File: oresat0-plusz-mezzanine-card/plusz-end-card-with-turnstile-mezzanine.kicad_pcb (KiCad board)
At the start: 8 copper layers, 83 x 84.4 mm, 37 parts, among them J1 R107064070, J10 R107064070, J2 R107064070, J3 R107064070, J4 R107064070, J5 R107064070, J6 R107064070, J7 R107064070, J8 R107064070, J9 R107064070, U1 QBA-07+, U2 QBA-07+, U3 QBA-07+, U7 QCN-19+, U8 QCN-19+, U9 QCN-19+

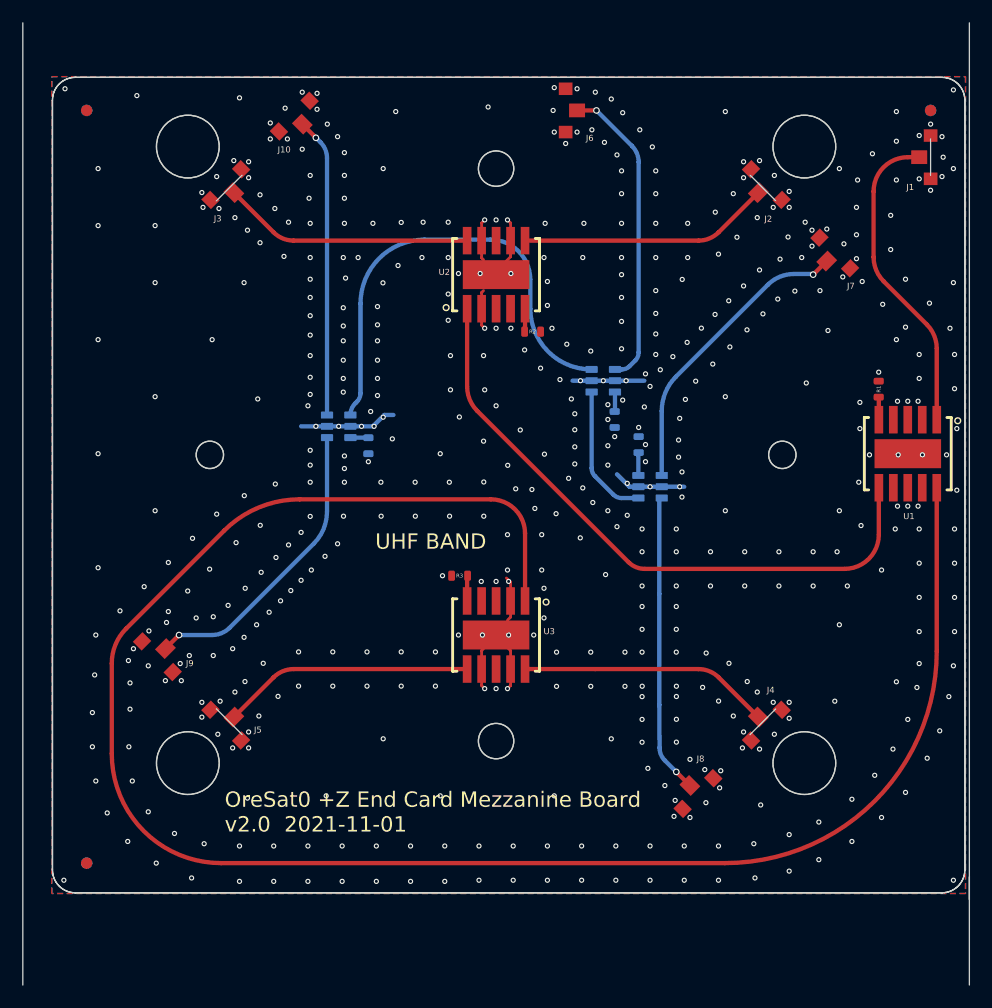
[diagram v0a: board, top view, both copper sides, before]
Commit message: Fixed Board Outline
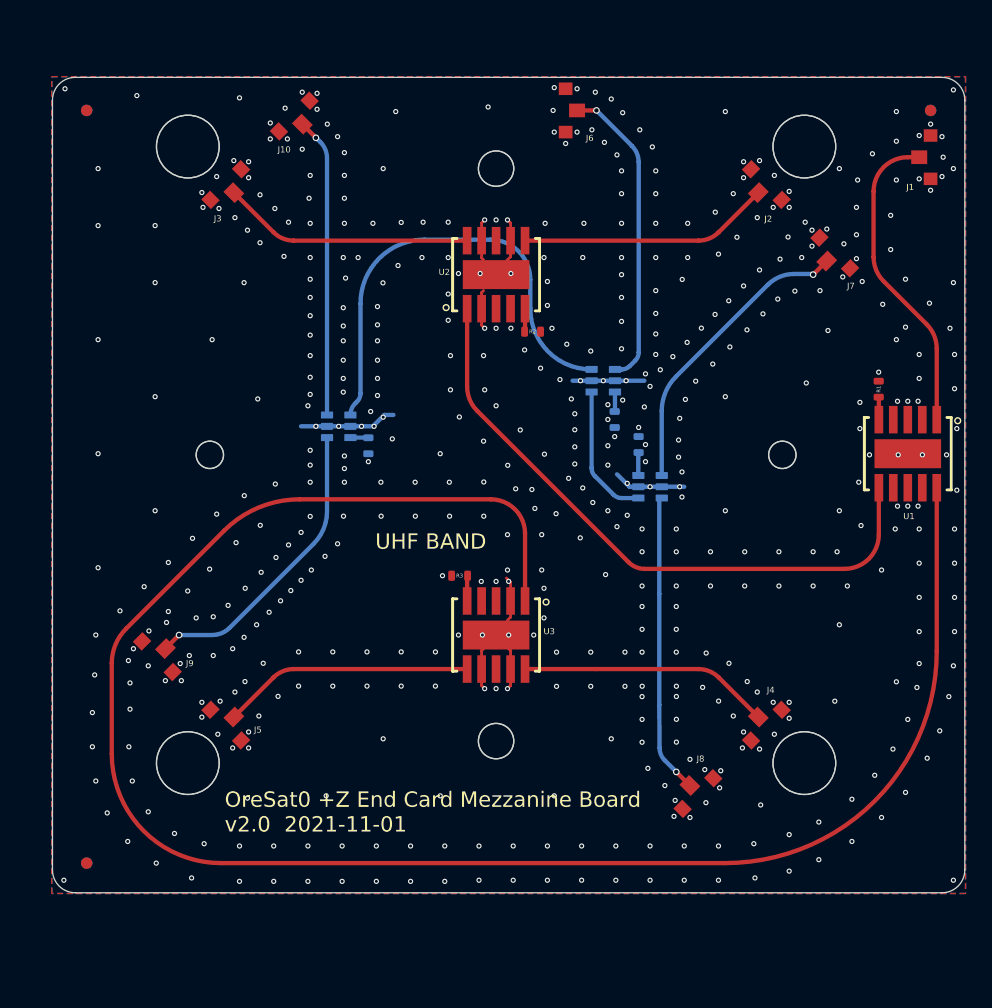
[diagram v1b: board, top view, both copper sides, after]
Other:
- board size 83 x 84.4 mm -> 80 x 71.5 mm
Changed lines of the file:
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@@
 		(descr "0603 (metric 1608) tight 'IPC-C' without silkscreen\nIn house package for minimum spacing based on IPC-7351B. This package is identical to 0603-C, but has its tPlace silkscreen layer removed.")
 		(property "Reference" "R5"
-			(at 0 0 -90)
+			(at 0 0 270)
 			(unlocked yes)
 			(layer "B.SilkS")
@@
 		)
 		(property "Value" "50"
-			(at -1.5 -1.8 -90)
+			(at -1.5 -1.8 270)
 			(unlocked yes)
 			(layer "B.Fab")
@@
 		)
 		(property "Datasheet" ""
-			(at 0 0 -90)
+			(at 0 0 270)
 			(layer "B.Fab")
 			(hide yes)
@@
 		)
 		(property "Description" ""
-			(at 0 0 -90)
+			(at 0 0 270)
 			(layer "B.Fab")
 			(hide yes)
@@
 		(at 134.7011 98.198579 -90)
 		(property "Reference" "U9"
-			(at -0.5 2.6 -0)
+			(at -0.5 2.6 0)
 			(unlocked yes)
 			(layer "B.SilkS")
@@
 		)
 		(property "Value" "QCN-19+"
-			(at 3.3 -1.4 -0)
+			(at 3.3 -1.4 0)
 			(unlocked yes)
 			(layer "B.Fab")
@@
 		(descr "0603 (metric 1608) tight 'IPC-C' without silkscreen\nIn house package for minimum spacing based on IPC-7351B. This package is identical to 0603-C, but has its tPlace silkscreen layer removed.")
 		(property "Reference" "R4"
-			(at 0 0 -90)
+			(at 0 0 270)
 			(unlocked yes)
 			(layer "B.SilkS")
@@
 		)
 		(property "Value" "50"
-			(at -1.5 -1.8 -90)
+			(at -1.5 -1.8 270)
 			(unlocked yes)
 			(layer "B.Fab")
@@
 		)
 		(property "Datasheet" ""
-			(at 0 0 -90)
+			(at 0 0 270)
 			(layer "B.Fab")
 			(hide yes)
@@
 		)
 		(property "Description" ""
-			(at 0 0 -90)
+			(at 0 0 270)
 			(layer "B.Fab")
 			(hide yes)
@@
 		)
 		(fp_text user "${REFERENCE}"
-			(at 0 0 -90)
+			(at 0 0 270)
 			(unlocked yes)
 			(layer "B.Mask")
@@
 		(at 157.9011 94.198579 -90)
 		(property "Reference" "U7"
-			(at -0.7 2.7 -0)
+			(at -0.7 2.7 0)
 			(unlocked yes)
 			(layer "B.SilkS")
@@
 		)
 		(property "Value" "QCN-19+"
-			(at 3.3 -1.4 -0)
+			(at 3.3 -1.4 0)
 			(unlocked yes)
 			(layer "B.Fab")
@@
 		(descr "0603 (metric 1608) tight 'IPC-C' without silkscreen\nIn house package for minimum spacing based on IPC-7351B. This package is identical to 0603-C, but has its tPlace silkscreen layer removed.")
 		(property "Reference" "R6"
-			(at 0 0 -90)
+			(at 0 0 270)
 			(unlocked yes)
 			(layer "B.SilkS")
@@
 		)
 		(property "Value" "50"
-			(at -1.5 -1.8 -90)
+			(at -1.5 -1.8 270)
 			(unlocked yes)
 			(layer "B.Fab")
@@
 		)
 		(property "Datasheet" ""
-			(at 0 0 -90)
+			(at 0 0 270)
 			(layer "B.Fab")
 			(hide yes)
@@
 		)
 		(property "Description" ""
-			(at 0 0 -90)
+			(at 0 0 270)
 			(layer "B.Fab")
 			(hide yes)
@@
 		)
 		(fp_text user "${REFERENCE}"
-			(at 0 0 -90)
+			(at 0 0 270)
 			(unlocked yes)
 			(layer "B.Mask")
@@
 		(end 176.1011 100.698579)
 		(stroke
-			(width 0)
+			(width 0.1)
 			(type solid)
 		)
@@
 		(end 151.5011 125.798579)
 		(stroke
-			(width 0)
+			(width 0.1)
 			(type solid)
 		)
@@
 		(end 158.1011 70.498579)
 		(stroke
-			(width 0)
+			(width 0.1)
 			(type solid)
 		)
@@
 		(end 165.1011 128.498579)
 		(stroke
-			(width 0)
+			(width 0.1)
 			(type solid)
 		)
@@
 		(end 177.1011 84.898579)
 		(stroke
-			(width 0)
+			(width 0.1)
 			(type solid)
 		)
@@
 		(end 125.9011 100.698579)
 		(stroke
-			(width 0)
+			(width 0.1)
 			(type solid)
 		)
@@
 		(end 121.5011 116.498579)
 		(stroke
-			(width 0)
+			(width 0.1)
 			(type solid)
 		)
@@
 		(end 151.5011 75.598579)
 		(stroke
-			(width 0)
+			(width 0.1)
 			(type solid)
 		)
@@
 		(end 133.5011 72.898579)
 		(stroke
-			(width 0)
+			(width 0.1)
 			(type solid)
 		)
@@
 		(end 126.4011 100.698579)
 		(stroke
-			(width 0)
+			(width 0.1)
 			(type solid)
 		)
@@
 		(end 151.5011 75.598579)
 		(stroke
-			(width 0)
+			(width 0.1)
 			(type solid)
 		)
@@
 		(end 151.5011 125.798579)
 		(stroke
-			(width 0)
+			(width 0.1)
 			(type solid)
 		)
@@
 		(end 176.6011 100.698579)
 		(stroke
-			(width 0)
+			(width 0.1)
 			(type solid)
 		)
@@
 		(layer "B.Mask")
 	)
-	(gr_line
-		(start 109.6011 137.098579)
-		(end 109.6011 69.598579)
-		(stroke
-			(width 0.001)
-			(type solid)
-		)
-		(layer "Edge.Cuts")
-	)
 	(gr_circle
 		(center 123.40109 100.698589)
@@
 	)
 	(gr_line
-		(start 186.60109 72.998589)
-		(end 186.60109 76.198589)
-		(stroke
-			(width 0.001)
-			(type solid)
-		)
-		(layer "Edge.Cuts")
-	)
-	(gr_line
-		(start 173.032459 78.429961)
-		(end 170.769718 76.16722)
-		(stroke
-			(width 0.001)
-			(type solid)
-		)
-		(layer "Edge.Cuts")
-	)
-	(gr_line
-		(start 170.769718 125.229939)
-		(end 173.032459 122.967198)
-		(stroke
-			(width 0.001)
-			(type solid)
-		)
-		(layer "Edge.Cuts")
-	)
-	(gr_arc
-		(start 189.6011 137.098579)
-		(mid 189.015314 138.512793)
-		(end 187.6011 139.098579)
-		(stroke
-			(width 0.001)
-			(type solid)
-		)
-		(layer "Edge.Cuts")
-	)
-	(gr_arc
-		(start 187.6011 67.598579)
-		(mid 189.015314 68.184365)
-		(end 189.6011 69.598579)
-		(stroke
-			(width 0.001)
-			(type solid)
-		)
-		(layer "Edge.Cuts")
-	)
-	(gr_line
-		(start 189.6011 137.098579)
-		(end 189.6011 69.598579)
-		(stroke
-			(width 0.001)
-			(type solid)
-		)
-		(layer "Edge.Cuts")
-	)
-	(gr_line
-		(start 107.0011 62.815761)
-		(end 107.0011 147.191439)
-		(stroke
-			(width 0.001)
-			(type solid)
-		)
-		(layer "Edge.Cuts")
-	)
-	(gr_arc
-		(start 109.6011 69.598579)
-		(mid 110.186886 68.184365)
-		(end 111.6011 67.598579)
-		(stroke
-			(width 0.001)
-			(type solid)
-		)
-		(layer "Edge.Cuts")
-	)
-	(gr_line
-		(start 187.6011 139.098579)
-		(end 111.6011 139.098579)
-		(stroke
-			(width 0.001)
-			(type solid)
-		)
-		(layer "Edge.Cuts")
-	)
-	(gr_line
 		(start 189.6011 69.598579)
 		(end 189.6011 137.098579)
@@
 		(layer "Edge.Cuts")
 	)
-	(gr_line
-		(start 190.0011 137.698579)
-		(end 190.0011 139.698579)
-		(stroke
-			(width 0.001)
-			(type solid)
-		)
-		(layer "Edge.Cuts")
-	)
-	(gr_line
-		(start 123.96974 122.967198)
-		(end 126.232481 125.229939)
-		(stroke
-			(width 0.001)
-			(type solid)
-		)
-		(layer "Edge.Cuts")
-	)
 	(gr_arc
 		(start 187.6011 67.598579)
@@
 		(layer "Edge.Cuts")
 	)
-	(gr_line
-		(start 187.6011 67.598579)
-		(end 111.6011 67.598579)
-		(stroke
-			(width 0.001)
-			(type solid)
-		)
-		(layer "Edge.Cuts")
-	)
 	(gr_arc
 		(start 109.6011 69.598579)
@@
 		(layer "Edge.Cuts")
 	)
-	(gr_line
-		(start 190.0011 62.815761)
-		(end 190.0011 147.191439)
-		(stroke
-			(width 0.001)
-			(type solid)
-		)
-		(layer "Edge.Cuts")
-	)
 	(gr_circle
 		(center 175.5311 73.668579)
@@
 		(layer "Edge.Cuts")
 	)
-	(gr_line
-		(start 126.232481 76.16722)
-		(end 123.96974 78.429961)
-		(stroke
-			(width 0.001)
-			(type solid)
-		)
-		(layer "Edge.Cuts")
-	)
 	(gr_arc
 		(start 111.6011 139.098579)
@@
 		(layer "Edge.Cuts")
 	)
-	(gr_arc
-		(start 111.6011 139.098579)
-		(mid 110.186886 138.512793)
-		(end 109.6011 137.098579)
-		(stroke
-			(width 0.001)
-			(type solid)
-		)
-		(layer "Edge.Cuts")
-	)
 	(gr_circle
 		(center 148.5011 91.398579)
@@
 				(xy 124.173642 103.07622) (xy 124.465548 102.960647) (xy 124.740667 102.809399) (xy 124.99466 102.624862)
 				(xy 125.223522 102.409947) (xy 125.423642 102.168042) (xy 125.591867 101.902963) (xy 125.725541 101.61889)
-				(xy 125.822558 101.320304) (xy 125.881387 101.011912) (xy 125.9011 100.698579)
+				(xy 125.822558 101.320304) (xy 125.881387 101.011912)
 			)
 		)
@@
 				(xy 174.373642 103.07622) (xy 174.665548 102.960647) (xy 174.940667 102.809399) (xy 175.19466 102.624862)
 				(xy 175.423522 102.409947) (xy 175.623642 102.168042) (xy 175.791867 101.902963) (xy 175.925541 101.61889)
-				(xy 176.022558 101.320304) (xy 176.081387 101.011912) (xy 176.1011 100.698579)
+				(xy 176.022558 101.320304) (xy 176.081387 101.011912)
 			)
 		)
